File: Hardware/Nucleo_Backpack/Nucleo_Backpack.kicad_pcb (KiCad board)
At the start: 2 copper layers, 70 x 57.5 mm, 5 parts, among them J1 CN7, J2 CN10

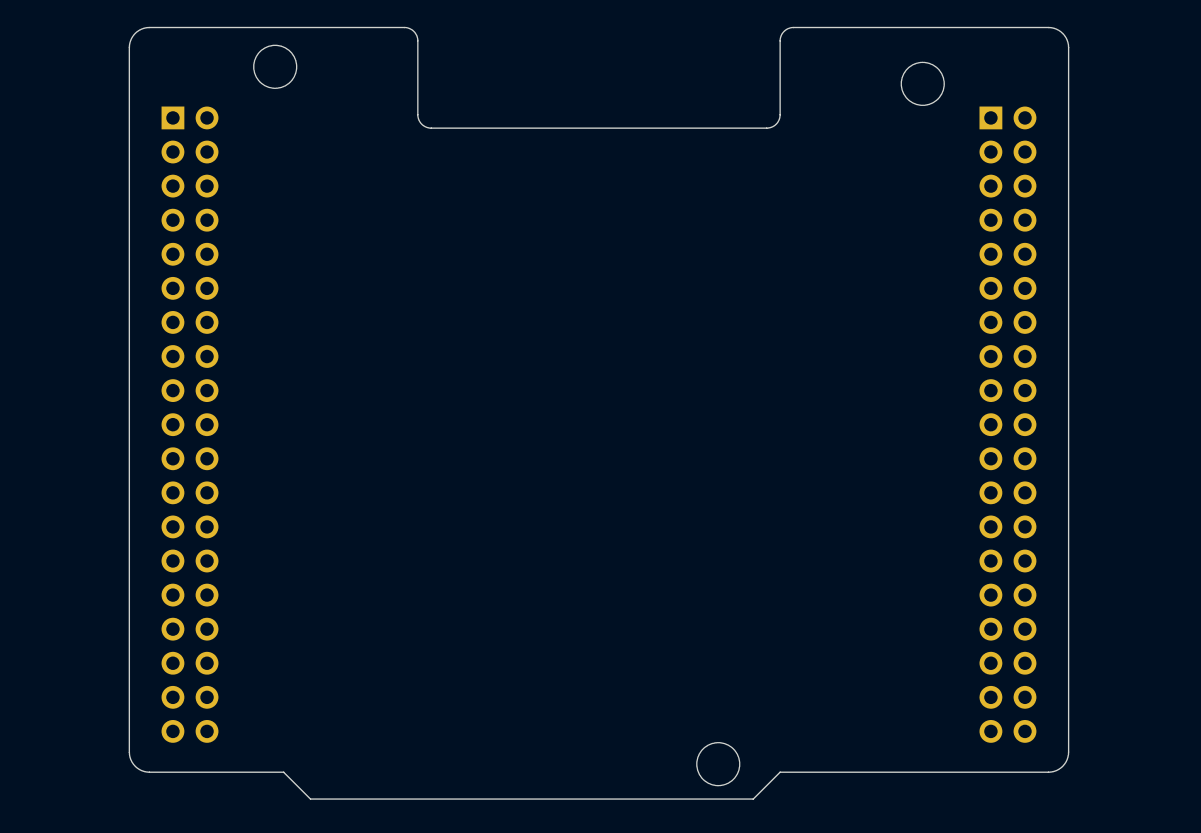
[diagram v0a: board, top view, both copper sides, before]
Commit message: Added Components to PCB for Backpack
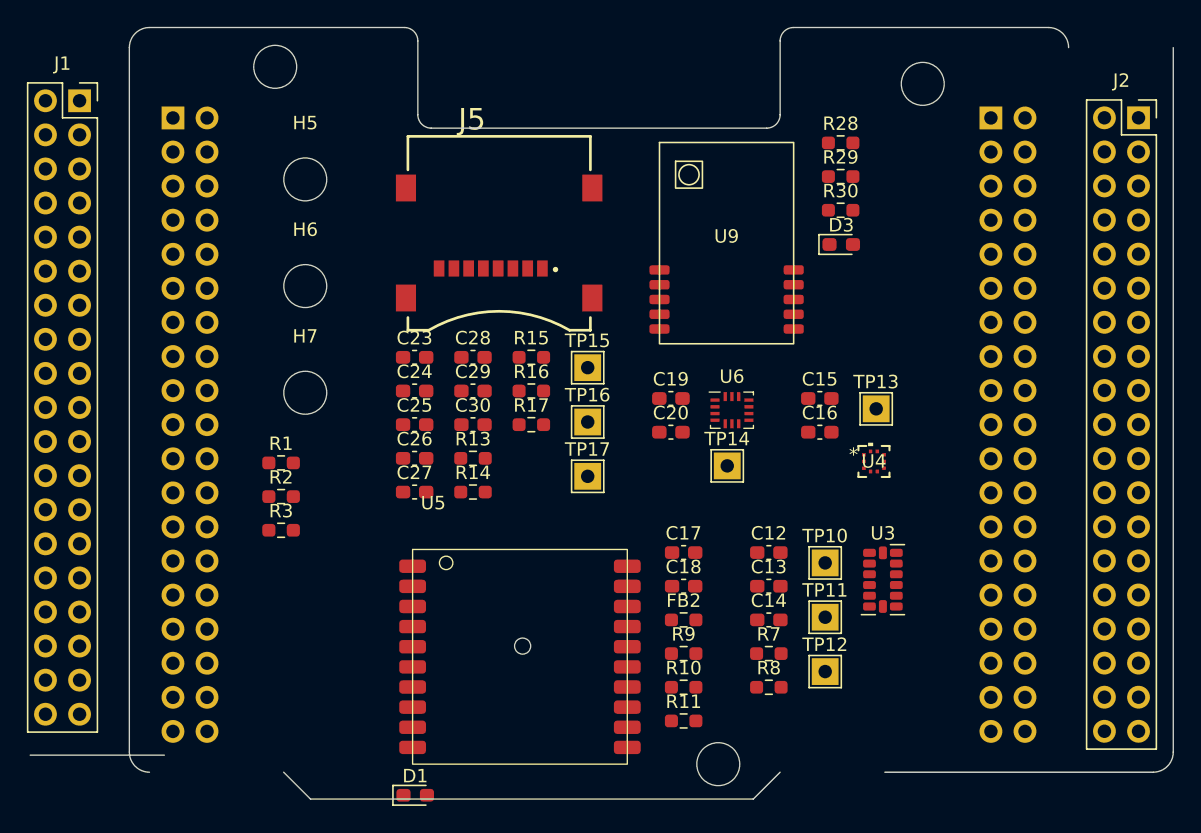
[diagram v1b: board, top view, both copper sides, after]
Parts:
- added C12: 100n, Capacitor_SMD:C_0603_1608Metric_Pad1.08x0.95mm_HandSolder, F.Cu at (149.2, 94.6)
- added C13: 100n, Capacitor_SMD:C_0603_1608Metric_Pad1.08x0.95mm_HandSolder, F.Cu at (149.2, 97.1)
- added C14: 10u, Capacitor_SMD:C_0603_1608Metric_Pad1.08x0.95mm_HandSolder, F.Cu at (149.2, 99.7)
- added C15: 100n, Capacitor_SMD:C_0603_1608Metric_Pad1.08x0.95mm_HandSolder, F.Cu at (153.0, 83.2)
- added C16: 100n, Capacitor_SMD:C_0603_1608Metric_Pad1.08x0.95mm_HandSolder, F.Cu at (153.0, 85.7)
- added C17: 1u, Capacitor_SMD:C_0603_1608Metric_Pad1.08x0.95mm_HandSolder, F.Cu at (142.8, 94.6)
- added C18: 100n, Capacitor_SMD:C_0603_1608Metric_Pad1.08x0.95mm_HandSolder, F.Cu at (142.8, 97.1)
- added C19: 100n, Capacitor_SMD:C_0603_1608Metric_Pad1.08x0.95mm_HandSolder, F.Cu at (141.9, 83.2)
- added C20: 100n, Capacitor_SMD:C_0603_1608Metric_Pad1.08x0.95mm_HandSolder, F.Cu at (141.9, 85.7)
- added C23: 22p, Capacitor_SMD:C_0603_1608Metric_Pad1.08x0.95mm_HandSolder, F.Cu at (122.8, 80.1)
- added C24: 22p, Capacitor_SMD:C_0603_1608Metric_Pad1.08x0.95mm_HandSolder, F.Cu at (122.8, 82.6)
- added C25: 22p, Capacitor_SMD:C_0603_1608Metric_Pad1.08x0.95mm_HandSolder, F.Cu at (122.8, 85.1)
- added C26: 22p, Capacitor_SMD:C_0603_1608Metric_Pad1.08x0.95mm_HandSolder, F.Cu at (122.8, 87.6)
- added C27: 10u, Capacitor_SMD:C_0603_1608Metric_Pad1.08x0.95mm_HandSolder, F.Cu at (122.8, 90.1)
- added C28: 22p, Capacitor_SMD:C_0603_1608Metric_Pad1.08x0.95mm_HandSolder, F.Cu at (127.1, 80.1)
- added C29: 22p, Capacitor_SMD:C_0603_1608Metric_Pad1.08x0.95mm_HandSolder, F.Cu at (127.1, 82.6)
- added C30: 100n, Capacitor_SMD:C_0603_1608Metric_Pad1.08x0.95mm_HandSolder, F.Cu at (127.1, 85.1)
- added D1: GPS_TX, LED_SMD:LED_0603_1608Metric_Pad1.05x0.95mm_HandSolder, F.Cu at (122.8, 112.7)
- added D3: BUSY, LED_SMD:LED_0603_1608Metric_Pad1.05x0.95mm_HandSolder, F.Cu at (154.6, 71.7)
- added FB2: FerriteBead, Resistor_SMD:R_0603_1608Metric_Pad0.98x0.95mm_HandSolder, F.Cu at (142.8, 99.7)
- added H5: MountingHole, MountingHole:MountingHole_3.2mm_M3, F.Cu at (114.6, 66.8)
- added H6: MountingHole, MountingHole:MountingHole_3.2mm_M3, F.Cu at (114.6, 74.8)
- added H7: MountingHole, MountingHole:MountingHole_3.2mm_M3, F.Cu at (114.6, 82.7)
- added J1: CN7, Connector_PinSocket_2.54mm:PinSocket_2x19_P2.54mm_Vertical, F.Cu at (97.8, 61.0)
- added J2: CN10, Connector_PinSocket_2.54mm:PinSocket_2x19_P2.54mm_Vertical, F.Cu at (176.7, 62.2)
- added J5: MEM2067-02-180-00-A_REVB, Project:GCT_MEM2067-02-180-00-A_REVB, F.Cu at (129.1, 70.8)
- added R1: 22k, Resistor_SMD:R_0603_1608Metric_Pad0.98x0.95mm_HandSolder, F.Cu at (112.8, 88.0)
- added R10: 220, Resistor_SMD:R_0603_1608Metric_Pad0.98x0.95mm_HandSolder, F.Cu at (142.8, 104.7)
- added R11: 22k, Resistor_SMD:R_0603_1608Metric_Pad0.98x0.95mm_HandSolder, F.Cu at (142.8, 107.2)
- added R13: 10k, Resistor_SMD:R_0603_1608Metric_Pad0.98x0.95mm_HandSolder, F.Cu at (127.1, 87.6)
- added R14: 10k, Resistor_SMD:R_0603_1608Metric_Pad0.98x0.95mm_HandSolder, F.Cu at (127.1, 90.1)
- added R15: 10k, Resistor_SMD:R_0603_1608Metric_Pad0.98x0.95mm_HandSolder, F.Cu at (131.5, 80.1)
- added R16: 10k, Resistor_SMD:R_0603_1608Metric_Pad0.98x0.95mm_HandSolder, F.Cu at (131.5, 82.6)
- added R17: 10k, Resistor_SMD:R_0603_1608Metric_Pad0.98x0.95mm_HandSolder, F.Cu at (131.5, 85.1)
- added R2: 22k, Resistor_SMD:R_0603_1608Metric_Pad0.98x0.95mm_HandSolder, F.Cu at (112.8, 90.5)
- added R28: 22k, Resistor_SMD:R_0603_1608Metric_Pad0.98x0.95mm_HandSolder, F.Cu at (154.5, 64.1)
- added R29: 10k, Resistor_SMD:R_0603_1608Metric_Pad0.98x0.95mm_HandSolder, F.Cu at (154.5, 66.6)
- added R3: 22k, Resistor_SMD:R_0603_1608Metric_Pad0.98x0.95mm_HandSolder, F.Cu at (112.8, 93.0)
- added R30: 22k, Resistor_SMD:R_0603_1608Metric_Pad0.98x0.95mm_HandSolder, F.Cu at (154.5, 69.1)
- added R7: 4.7k, Resistor_SMD:R_0603_1608Metric_Pad0.98x0.95mm_HandSolder, F.Cu at (149.2, 102.2)
- added R8: 4.7k, Resistor_SMD:R_0603_1608Metric_Pad0.98x0.95mm_HandSolder, F.Cu at (149.2, 104.7)
- added R9: 220, Resistor_SMD:R_0603_1608Metric_Pad0.98x0.95mm_HandSolder, F.Cu at (142.8, 102.2)
- added TP10: SDA, TestPoint:TestPoint_THTPad_2.0x2.0mm_Drill1.0mm, F.Cu at (153.4, 95.4)
- added TP11: SCL, TestPoint:TestPoint_THTPad_2.0x2.0mm_Drill1.0mm, F.Cu at (153.4, 99.5)
- added TP12: ACC_INT, TestPoint:TestPoint_THTPad_2.0x2.0mm_Drill1.0mm, F.Cu at (153.4, 103.5)
- added TP13: BARO_INT, TestPoint:TestPoint_THTPad_2.0x2.0mm_Drill1.0mm, F.Cu at (157.2, 83.9)
- added TP14: IMU_INT, TestPoint:TestPoint_THTPad_2.0x2.0mm_Drill1.0mm, F.Cu at (146.1, 88.2)
- added TP15: SD_CLK, TestPoint:TestPoint_THTPad_2.0x2.0mm_Drill1.0mm, F.Cu at (135.7, 80.8)
- added TP16: SD_CMD, TestPoint:TestPoint_THTPad_2.0x2.0mm_Drill1.0mm, F.Cu at (135.7, 84.9)
- added TP17: SD_D0, TestPoint:TestPoint_THTPad_2.0x2.0mm_Drill1.0mm, F.Cu at (135.7, 89.0)
- added U3: ADXL375, Package_LGA:LGA-14_3x5mm_P0.8mm_LayoutBorder1x6y, F.Cu at (157.7, 96.7)
- added U4: BMP390, Project:LGA10_BMP390_BOS, F.Cu at (157.0, 87.8)
- added U5: FGPMMOPA6H, Project:FGPMMOPA6H, F.Cu at (122.6, 94.4)
- added U6: BMI323, Package_LGA:Bosch_LGA-14_3x2.5mm_P0.5mm, F.Cu at (146.4, 84.0)
- added U9: LR62E, Project:LR62E, F.Cu at (146.0, 71.6)
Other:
- board size 70 x 57.5 mm -> 85.2 x 57.5 mm

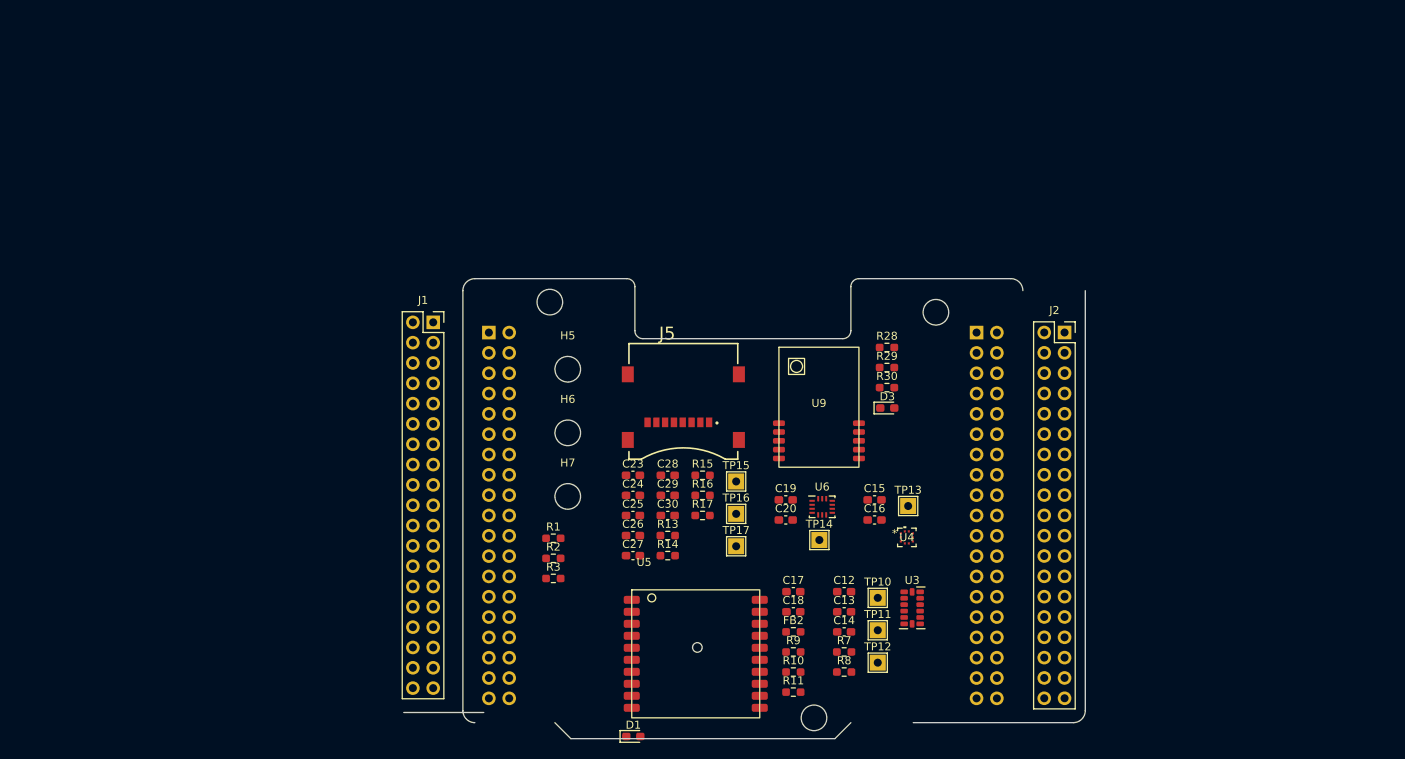
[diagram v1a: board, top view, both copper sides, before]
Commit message: all components now on the backpack
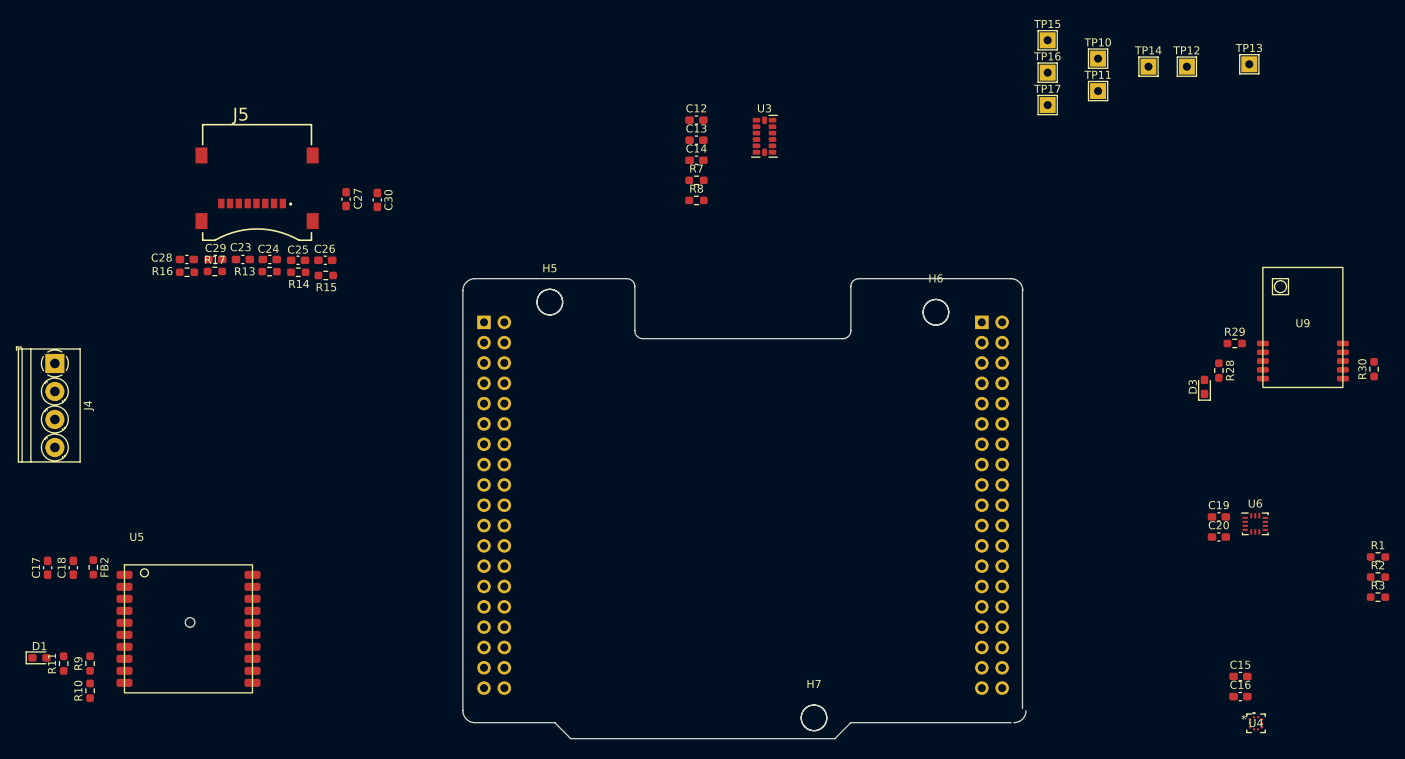
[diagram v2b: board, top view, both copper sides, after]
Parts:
- removed the J1 at (104.8, 62.2)
- removed the J2 at (165.7, 62.2)
- added J4: Conn_01x04, TerminalBlock_Phoenix:TerminalBlock_Phoenix_PT-1,5-4-3.5-H_1x04_P3.50mm_Horizontal, F.Cu at (50.5, 66.1)
- J1, J2: moved to B.Cu
- moved R1 103.1 mm to (215.9, 90.3)
- moved R2 103.1 mm to (215.9, 92.8)
- moved R3 103.1 mm to (215.9, 95.3)
- moved C17 93.3 mm to (49.6, 91.6), turned to 90 degrees
- moved R11 91.3 mm to (51.6, 103.6), turned to 90 degrees
- moved C18 90.2 mm to (52.8, 91.6), turned to 90 degrees
- moved R10 87.9 mm to (54.9, 107.0), turned to 90 degrees
- moved R9 87.9 mm to (54.9, 103.6), turned to 90 degrees
- moved FB2 87.9 mm to (55.3, 91.6), turned to -90 degrees
- moved TP12 83.9 mm to (192.0, 29.0)
- moved D1 74.9 mm to (48.6, 102.9)
- moved TP10 72.8 mm to (180.9, 28.0)
- moved TP11 72.8 mm to (180.9, 32.0)
- moved TP14 72.1 mm to (187.2, 29.0)
- moved R16 70.2 mm to (67.0, 54.7)
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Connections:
- J2 pad 33: unconnected-(J2-Pin_33-Pad33) -> USART1_RX
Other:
- board size 85.2 x 57.5 mm -> 70.4 x 57.5 mm

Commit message: Backpack done except grounding
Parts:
- moved J4 98.4 mm to (141.6, 103.1), turned to 90 degrees
- moved TP12 85.2 mm to (162.5, 109.0)
- moved TP15 78.3 mm to (113.0, 74.0)
- moved TP13 73.8 mm to (161.8, 92.0), turned to 180 degrees
- moved R3 73.8 mm to (143.5, 81.1)
- moved TP16 71.0 mm to (113.5, 66.0)
- moved C28 69.1 mm to (134.9, 66.0), turned to 0 degrees
- moved R16 68.6 mm to (134.9, 64.4), turned to 180 degrees
- moved R2 65.6 mm to (150.4, 96.4), turned to 180 degrees
- moved TP14 64.4 mm to (160.4, 87.6)
- moved C17 62.7 mm to (112.3, 90.2)
- moved D1 62.6 mm to (111.1, 101.3)
- moved R11 62.3 mm to (113.9, 102.3)
- moved U4 62.3 mm to (143.0, 87.5)
- moved C29 62.1 mm to (131.3, 66.0), turned to 0 degrees
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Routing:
- net +3.3V: track 0.00 -> 219.4 mm, vias 0 -> 21
- net SPI2_MISO: track 0.00 -> 83.5 mm, vias 0 -> 3
- net SPI2_MOSI: track 0.00 -> 79.6 mm, vias 0 -> 2
- net RADIO_DIO1: track 0.00 -> 70.0 mm
- net USART1_RX: track 0.11 -> 65.4 mm
- net USART1_TX: track 0.00 -> 59.4 mm, vias 0 -> 2
- net SDIO_D0: track 0.00 -> 55.9 mm, vias 0 -> 2
- net RADIO_RST: track 0.00 -> 54.0 mm, vias 0 -> 2
- net ACCEL_INT: track 0.00 -> 51.0 mm, vias 0 -> 1
- net SPI2_CS2: track 0.00 -> 46.1 mm
- net SDIO_D1: track 0.00 -> 43.9 mm
- net SDIO_CK: track 0.00 -> 39.1 mm
- net SDIO_CMD: track 0.00 -> 36.2 mm
- net SPI2_CS1: track 0.00 -> 31.0 mm
- net SPI2_SCK: track 0.00 -> 29.9 mm, vias 0 -> 2
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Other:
- board size 70.4 x 57.5 mm -> 70.1 x 57.5 mm
